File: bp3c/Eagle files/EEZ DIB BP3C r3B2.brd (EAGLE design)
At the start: 110 x 90 mm, 62 parts, among them IC1 TCA9534PWR, Q1 2N7002, Q2 2N7002, Q3 2N7002, Q4 2N7002, X1 ZL202-20G, X2 ZL202-20G, X3 ZL202-20G, X4 DS1022-2*20RF11, X5 DS1023-2*14S21, X6 DS1023-2*14S21, X7 DS1023-2*14S21, X8 N.C.

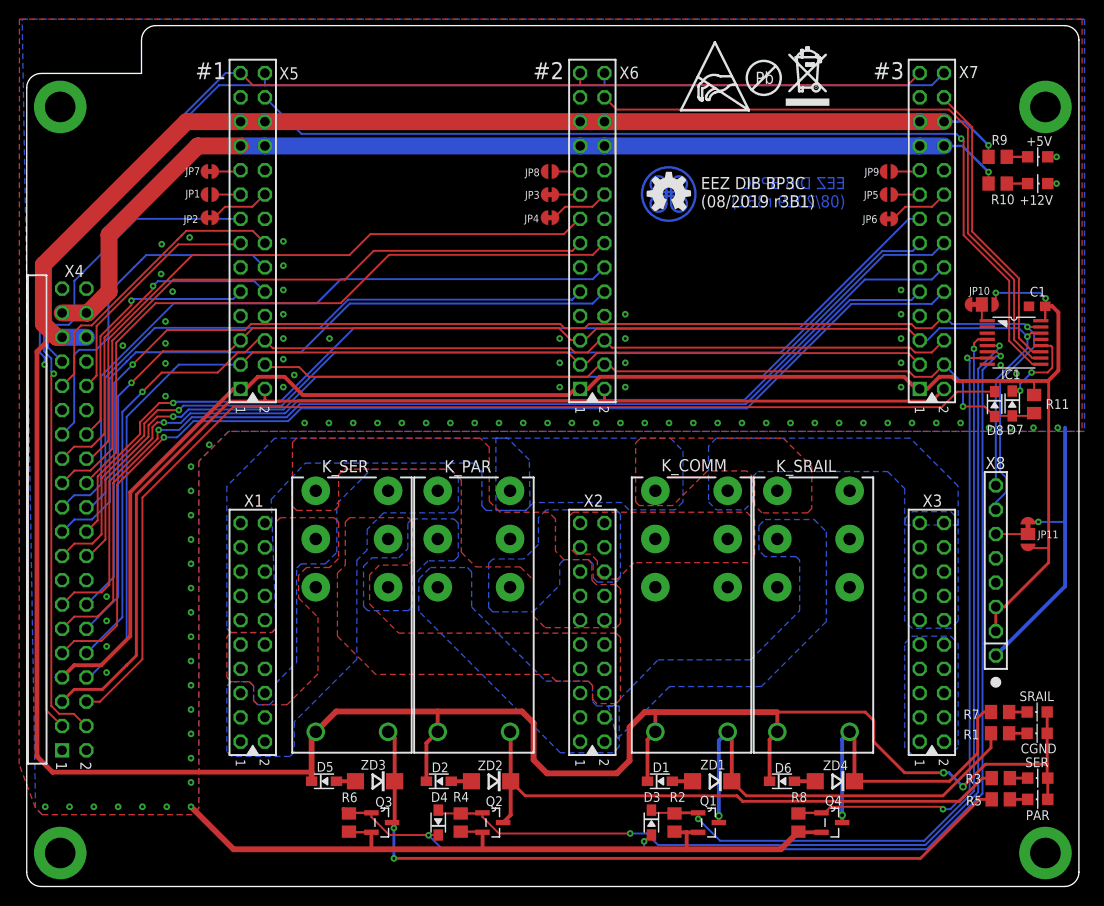
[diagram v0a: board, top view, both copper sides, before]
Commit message: BP3C reset fix
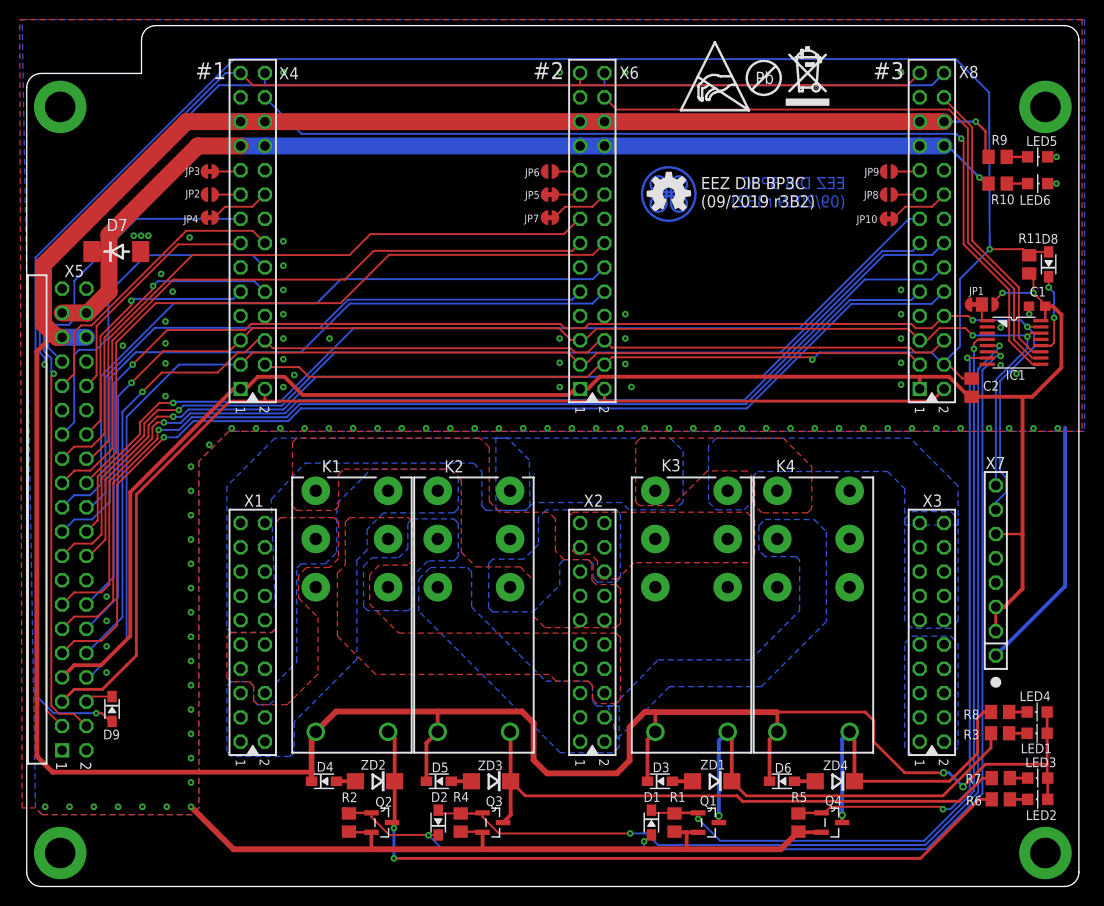
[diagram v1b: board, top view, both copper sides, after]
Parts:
- removed JP11: JP3-CUT, EEZ_Lib1:JP3-CUT
- removed K_COMM: RT424005, EEZ_Lib1:RT-C/016A5_ROUND
- added C2: 1n, rcl:C0805
- added D9: BAS316, EEZ_Lib1:SOD323-R
- added K3: RT424005, EEZ_Lib1:RT-C/016A5_ROUND
- D1, D2: value BAS316 -> N.C.
- D3, D4: value N.C. -> BAS316
- D7: value BAS316 -> N.C.; device EEZ_Lib1:SOD323-R -> MyLib6:DO214AA
- JP1: value JP2-CUT -> JP3-CUT; device EEZ_Lib1:JP2-CUT -> EEZ_Lib1:JP3-CUT
- JP10: value JP3-CUT -> JP2-NOCUT; device EEZ_Lib1:JP3-CUT -> EEZ_Lib1:JP2-NOCUT
- JP2, JP6: value JP2-NOCUT -> JP2-CUT; device EEZ_Lib1:JP2-NOCUT -> EEZ_Lib1:JP2-CUT
- JP5: value JP2-CUT -> JP2-NOCUT; device EEZ_Lib1:JP2-CUT -> EEZ_Lib1:JP2-NOCUT
- R1, R5: value N.C. -> 100K
- R6, R8: value 100K -> N.C.
- X4: value DS1022-2*20RF11 -> DS1023-2*14S21; device EEZ_connectors:ZL212-40KG -> EEZ_connectors:TSW-114-07-F-D
- X5: value DS1023-2*14S21 -> DS1022-2*20RF11; device EEZ_connectors:TSW-114-07-F-D -> EEZ_connectors:ZL212-40KG
- X7: value DS1023-2*14S21 -> N.C.; device EEZ_connectors:TSW-114-07-F-D -> con-samtec:SSW-108-02-S-S
- X8: value N.C. -> DS1023-2*14S21; device con-samtec:SSW-108-02-S-S -> EEZ_connectors:TSW-114-07-F-D
- moved D7 95.0 mm to (-0.64, 71.4), turned to 0 degrees
- moved JP1 81.5 mm to (89.9, 65.8)
- moved R6 68.2 mm to (91.8, 14.1), turned to 180 degrees
- moved X7 52.6 mm to (91.3, 38.0), turned to 90 degrees
- moved X8 52.6 mm to (83.4, 90.0), turned to 270 degrees
- moved JP7 35.9 mm to (44.7, 74.9), turned to 180 degrees
- moved JP6 35.8 mm to (44.7, 79.7), turned to 0 degrees
- moved JP3 35.6 mm to (9.14, 79.7)
- moved JP4 35.6 mm to (9.14, 74.9)
- moved JP8 35.5 mm to (80.1, 77.3)
- moved JP5 35.4 mm to (44.7, 77.3)
- moved R1 35.3 mm to (57.7, 11.7), turned to 90 degrees
- moved R2 34.0 mm to (23.7, 11.7)
- moved X4 29.3 mm to (12.4, 90.0)
- moved X5 29.3 mm to (-6.30, 67.5)
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- renumbered +12V to LED6, +5V to LED5, CGND to LED1, K_PAR to K2, K_SER to K1, K_SRAIL to K4, PAR to LED2, SER to LED3, SRAIL to LED4
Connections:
- removed net ALT_ADDR: JP11.COM, X8.6
- removed net N$128 (its old number): D2.A, ZD2.A
- new net N$104: D4.A, ZD2.A
- net !FAULT: now also X4.3, X5.8, X8.3; no longer X4.8, X5.3, X7.3
- net !MRESET: now also D9.C, X5.6; no longer D8.C, X4.6
- net !RESET: now also C2.1, D9.A, X4.4, X8.4; no longer D7.A, X5.4, X7.4
- net +12V: now also D7.C, X4.21, X4.22, X5.37, X5.38, X8.21, X8.22; no longer X4.37, X4.38, X5.21, X5.22, X7.21, X7.22
- net +3V3: now also C2.2, JP1.NO, X4.1, X5.7, X7.2, X7.3, X7.6, X8.1; no longer JP10.NO, JP11.NO, X4.7, X5.1, X7.1, X8.2, X8.3
- net +5V: now also D3.C, D4.C, K3.A2, X4.23, X4.24, X5.35, X5.36, X8.23, X8.24; no longer D1.C, D2.C, K_COMM.A2, X4.35, X4.36, X5.23, X5.24, X7.23, X7.24
- net +VAUX: now also X4.2, X5.5, X8.2; no longer X4.5, X5.2, X7.2
- net BOOT1: now also X4.26; no longer X5.26
- net BOOT3: now also X8.26; no longer X7.26
- net CH1_OUT-: now also K3.14A; no longer K_COMM.14A
- net CH2_OUT-: now also K3.11A, K3.11B; no longer K_COMM.11A, K_COMM.11B
- net CH3-: now also K3.14B; no longer K_COMM.14B
- net GND: now also D7.A, JP1.NC, JP10.2, JP2.1, JP6.1, JP7.2, R1.1, R5.1, X4.11, X4.25, X4.7, X5.1, X5.15, X5.2, X5.29, X5.30, X5.34, X5.39, X5.40, X7.1, X8.11, X8.16, X8.25, X8.7; no longer JP1.1, JP10.NC, JP11.NC, JP2.2, JP6.2, JP7.1, R6.1, R8.1, X4.1, X4.15, X4.2, X4.29, X4.30, X4.34, X4.39, X4.40, X5.11, X5.25, X5.7, X7.11, X7.16, X7.25, X7.7, X8.1
- net I2C1_SCL: now also X4.5, X5.12, X7.8, X8.5; no longer X4.12, X5.5, X7.5, X8.8
- net I2C1_SDA: now also X4.8, X5.14, X7.7, X8.8; no longer X4.14, X5.8, X7.8, X8.7
- net N$10: now also JP5.2; no longer JP3.2
- net N$101: now also Q2.3, R6.2, ZD2.C; no longer Q3.3, R5.2, ZD3.C
- net N$102: now also Q3.3, R7.2, ZD3.C; no longer Q2.3, R3.2, ZD2.C
- net N$11: now also JP6.2; no longer JP8.2
- net N$12: now also JP10.1, X8.18; no longer JP6.1, X7.18
- net N$13: now also JP8.2, X8.17; no longer JP5.2, X7.17
- net N$14: now also X8.19; no longer X7.19
- net N$15: now also JP1.COM; no longer JP10.COM
- net N$17: now also K3.A1, R3.2; no longer K_COMM.A1, R1.2
- net N$18: now also D3.A; no longer D1.A
- net N$19: now also R3.1; no longer R1.1
- net N$2: now also JP4.1, X4.18; no longer JP2.1, X5.18
- net N$20: now also R8.2; no longer R7.2
- net N$22: now also R8.1; no longer R7.1
- net N$5: now also JP2.2, X4.17; no longer JP1.2, X5.17
- net N$6: now also JP3.2, X4.19; no longer JP7.2, X5.19
- net N$7: now also R6.1; no longer R5.1
- net N$8: now also R7.1; no longer R3.1
- net N$9: now also JP7.1; no longer JP4.1
- net OE_SYNC: now also X4.6, X5.10, X8.6; no longer X4.10, X5.6, X7.6
- net OUT_CGND: now also D1.C, R1.2; no longer D3.C, R2.2
- net OUT_PAR: now also D2.A, Q3.1; no longer D4.A, Q2.1
- net OUT_SER: now also D1.A, D2.C, Q2.1, R2.2; no longer D3.A, D4.C, Q3.1, R6.2
- net OUT_SRA: now also R5.2; no longer R8.2
- net PROG_RST: now also D8.C; no longer D7.C
- net SPI2_CLK: now also X4.13, X5.32; no longer X4.32, X5.13
- net SPI2_CSA: now also X4.9, X5.28; no longer X4.28, X5.9
- net SPI2_CSB: now also X4.12, X5.27; no longer X4.27, X5.12
- net SPI2_IRQ: now also X4.10, X5.25; no longer X4.25, X5.10
- net SPI2_MISO: now also X4.14, X5.31; no longer X4.31, X5.14
- net SPI2_MOSI: now also X4.15, X5.33; no longer X4.33, X5.15
- net SPI4_CLK: now also X5.23; no longer X4.23
- net SPI4_CSA: now also X5.22; no longer X4.22
- net SPI4_CSB: now also X5.21; no longer X4.21
- net SPI4_IRQ: now also X5.19; no longer X4.19
- net SPI4_MISO: now also X5.24; no longer X4.24
- net SPI4_MOSI: now also X5.26; no longer X4.26
- net SPI5_CLK: now also X5.17, X8.13; no longer X4.17, X7.13
- net SPI5_CSA: now also X5.11, X8.9; no longer X4.11, X7.9
- net SPI5_CSB: now also X5.13, X8.12; no longer X4.13, X7.12
- net SPI5_IRQ: now also X5.9, X8.10; no longer X4.9, X7.10
- net SPI5_MISO: now also X5.18, X8.14; no longer X4.18, X7.14
- net SPI5_MOSI: now also X5.20, X8.15; no longer X4.20, X7.15
- net UART_RX: now also X4.27, X5.3, X8.27; no longer X4.3, X5.27, X7.27
- net UART_TX: now also X4.28, X5.4, X8.28; no longer X4.4, X5.28, X7.28
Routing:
- net !RESET: track 86.3 -> 279.0 mm, vias 1 -> 3
- net !MRESET: track 118.3 -> 2.90 mm
- net GND: track 111.8 -> 107.9 mm, vias 93 -> 103
- net ALT_ADDR: track 3.37 -> 0.00 mm
- net N$128 (its old number): track 2.11 -> 0.00 mm
- net N$104: track 0.00 -> 1.98 mm
- net +3V3: track 180.2 -> 178.9 mm
- net +12V: track 109.9 -> 111.2 mm
- net +5V: track 322.7 -> 323.5 mm
- net I2C1_SDA: track 148.6 -> 149.1 mm, vias 2 -> 3
- net I2C1_SCL: track 144.8 -> 144.5 mm, vias 2 -> 3
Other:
- board text added: "EEZ DIB BP3C (09/2019 r3B2)"
- board text removed: "EEZ DIB BP3C (08/2019 r3B1)"

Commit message: add OSHWA ID on BP3C PCB
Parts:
- added OSHWA: HR000002, EEZ_Lib1:CERT-SMALL-SILK
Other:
- board text added: "EEZ DIB BP3C (01/2020 r3B2)"
- board text added: "Project source code: github.com/eez-open"
- board text removed: "EEZ DIB BP3C (09/2019 r3B2)"
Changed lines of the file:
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@@
 <grid distance="2.5" unitdist="mil" unit="mil" style="lines" multiple="20" display="no" altdistance="12.5" altunitdist="mil" altunit="mil"/>
 <layers>
-<layer number="1" name="Top" color="11" fill="1" visible="no" active="yes"/>
+<layer number="1" name="Top" color="11" fill="1" visible="yes" active="yes"/>
 <layer number="2" name="Gnd" color="2" fill="1" visible="no" active="no"/>
 <layer number="3" name="Route3" color="4" fill="3" visible="no" active="no"/>
@@
 <layer number="14" name="Route14" color="1" fill="6" visible="no" active="no"/>
 <layer number="15" name="Power" color="7" fill="1" visible="no" active="no"/>
-<layer number="16" name="Bottom" color="1" fill="1" visible="no" active="yes"/>
-<layer number="17" name="Pads" color="6" fill="1" visible="no" active="yes"/>
-<layer number="18" name="Vias" color="6" fill="1" visible="no" active="yes"/>
+<layer number="16" name="Bottom" color="1" fill="1" visible="yes" active="yes"/>
+<layer number="17" name="Pads" color="6" fill="1" visible="yes" active="yes"/>
+<layer number="18" name="Vias" color="6" fill="1" visible="yes" active="yes"/>
 <layer number="19" name="Unrouted" color="6" fill="1" visible="no" active="yes"/>
 <layer number="20" name="Dimension" color="12" fill="1" visible="yes" active="yes"/>
 <layer number="21" name="tPlace" color="7" fill="1" visible="yes" active="yes"/>
 <layer number="22" name="bPlace" color="13" fill="1" visible="no" active="yes"/>
-<layer number="23" name="tOrigins" color="15" fill="1" visible="no" active="yes"/>
+<layer number="23" name="tOrigins" color="15" fill="1" visible="yes" active="yes"/>
 <layer number="24" name="bOrigins" color="15" fill="1" visible="no" active="yes"/>
 <layer number="25" name="tNames" color="7" fill="1" visible="yes" active="yes"/>
 <layer number="26" name="bNames" color="13" fill="1" visible="no" active="yes"/>
-<layer number="27" name="tValues" color="12" fill="1" visible="yes" active="yes"/>
+<layer number="27" name="tValues" color="12" fill="1" visible="no" active="yes"/>
 <layer number="28" name="bValues" color="11" fill="1" visible="no" active="yes"/>
 <layer number="29" name="tStop" color="15" fill="1" visible="yes" active="yes"/>
@@
 <rectangle x1="56.9655" y1="79.7249" x2="57.2055" y2="79.7287" layer="21"/>
 <text x="60.4762" y="75.9987" size="1.27" layer="21" font="vector" ratio="10" rot="SR0">EEZ DIB BP3C
-(09/2019 r3B2)</text>
+(01/2020 r3B2)</text>
 <text x="75.5937" y="75.9987" size="1.27" layer="16" font="vector" ratio="10" rot="SMR0">EEZ DIB BP3C
-(09/2019 r3B2)</text>
+(01/2020 r3B2)</text>
 <dimension x1="82" y1="43" x2="78.5" y2="90" x3="91.5" y3="66.5" textsize="1.778" layer="47" dtype="vertical"/>
 <dimension x1="83.4" y1="2.1" x2="85" y2="20.1" x3="79.473" y3="11.1" textsize="1.778" layer="47" dtype="vertical"/>
@@
 <wire x1="2" y1="93.5" x2="2" y2="90" width="0.1" layer="20"/>
 <wire x1="2" y1="90" x2="-8.5" y2="90" width="0.1" layer="20"/>
+<text x="8.0887" y="6.4662" size="1.27" layer="21" font="vector" ratio="10" rot="SR0">Project source code: github.com/eez-open</text>
 </plain>
 <attributes>
@@
 <attribute name="VALUE" x="-2.005" y="70.7" size="1.27" layer="27" ratio="10"/>
 </element>
+<element name="OSHWA" library="EEZ_Lib1" package="CERT-SMALL-SILK" value="HR000002" x="2.3495" y="8.128" smashed="yes">
+<attribute name="VALUE" x="-2.16344375" y="6.4135" size="1.27" layer="21" font="vector" ratio="12"/>
+</element>
 </elements>

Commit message: Centroid files added
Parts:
- added FM1, FM2: FIDUCIAL, EEZ_Lib1:FIDUCIAL
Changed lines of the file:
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@@
 <setting verticaltext="up"/>
 </settings>
-<grid distance="2.5" unitdist="mil" unit="mil" style="lines" multiple="20" display="no" altdistance="12.5" altunitdist="mil" altunit="mil"/>
+<grid distance="0.0635" unitdist="mm" unit="mm" style="lines" multiple="20" display="no" altdistance="12.5" altunitdist="mil" altunit="mil"/>
 <layers>
 <layer number="1" name="Top" color="11" fill="1" visible="yes" active="yes"/>
@@
 <attribute name="VALUE" x="-2.16344375" y="6.4135" size="1.27" layer="21" font="vector" ratio="12"/>
 </element>
+<element name="FM1" library="EEZ_Lib1" package="FIDUCIAL" value="FIDUCIAL" x="-2" y="88"/>
+<element name="FM2" library="EEZ_Lib1" package="FIDUCIAL" value="FIDUCIAL" x="91.5" y="7.5"/>
 </elements>
 <signals>
